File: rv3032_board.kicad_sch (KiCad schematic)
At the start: 7 parts, among them J1 Conn_01x05_Pin, U1 RV-3032

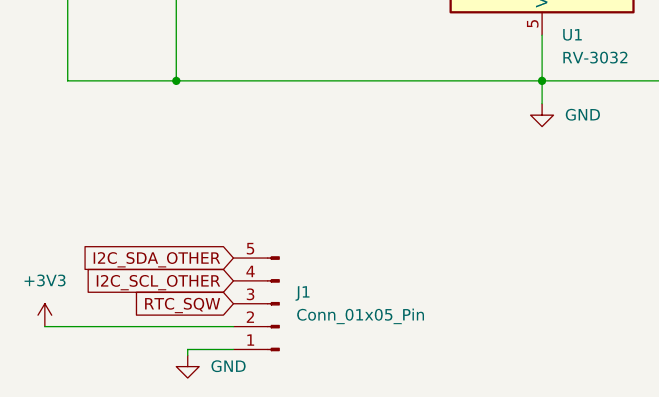
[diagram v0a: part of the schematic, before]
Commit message: v2: replacement DS3231
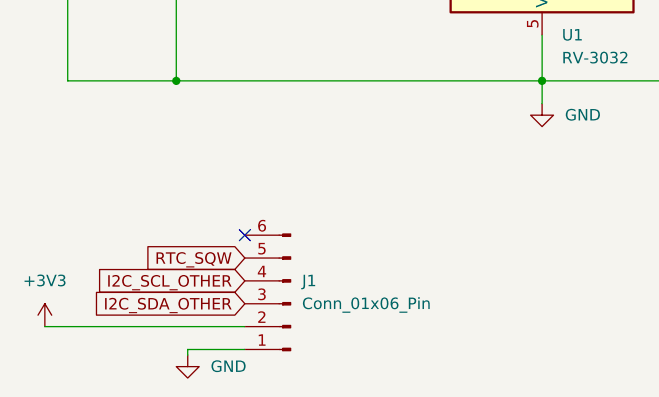
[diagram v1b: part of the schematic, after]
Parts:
- removed J1: Conn_01x05_Pin, Connector_PinHeader_2.54mm:PinHeader_1x05_P2.54mm_Horizontal, symbol Connector:Conn_01x05_Pin
- added J1: Conn_01x06_Pin, Connector_PinHeader_2.54mm:PinHeader_1x06_P2.54mm_Horizontal, symbol Connector:Conn_01x06_Pin
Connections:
- net +3V3: now also J1.2 (Pin_2)
- net GND: now also J1.1 (Pin_1)
- net I2C_SCL_OTHER: now also J1.4 (Pin_4)
- net I2C_SDA_OTHER: now also J1.3 (Pin_3)
- net RTC_SQW: now also J1.5 (Pin_5)
- no-connect marks 2 -> 3
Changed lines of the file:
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@@
   (no_connect (at 106.68 45.085))
   (no_connect (at 106.68 42.545))
+  (no_connect (at 60.96 74.93))
   (wire (pts (xy 93.98 57.785) (xy 93.98 52.705))
     (stroke (width 0) (type default))
@@
     (stroke (width 0) (type default))
   )
-  (wire (pts (xy 59.69 87.63) (xy 54.61 87.63))
+  (wire (pts (xy 54.61 87.63) (xy 60.96 87.63))
     (stroke (width 0) (type default))
   )
@@
     (stroke (width 0) (type default))
   )
-  (wire (pts (xy 38.735 85.09) (xy 59.69 85.09))
+  (wire (pts (xy 38.735 85.09) (xy 60.96 85.09))
     (stroke (width 0) (type default))
   )
@@
     (stroke (width 0) (type default))
   )
-  (global_label "I2C_SDA_OTHER" (shape input) (at 59.69 77.47 180) (fields_autoplaced)
+  (global_label "I2C_SDA_OTHER" (shape input) (at 60.96 82.55 180) (fields_autoplaced)
     (effects (font (size 1.27 1.27)) (justify right))
-    (property "Intersheetrefs" "${INTERSHEET_REFS}" (at 42.0696 77.47 0)
+    (property "Intersheetrefs" "${INTERSHEET_REFS}" (at 43.3396 82.55 0)
       (effects (font (size 1.27 1.27)) (justify right) hide)
     )
@@
     )
   )
-  (global_label "I2C_SCL_OTHER" (shape input) (at 59.69 80.01 180) (fields_autoplaced)
+  (global_label "I2C_SCL_OTHER" (shape input) (at 60.96 80.01 180) (fields_autoplaced)
     (effects (font (size 1.27 1.27)) (justify right))
-    (property "Intersheetrefs" "${INTERSHEET_REFS}" (at 42.1301 80.01 0)
+    (property "Intersheetrefs" "${INTERSHEET_REFS}" (at 43.4001 80.01 0)
       (effects (font (size 1.27 1.27)) (justify right) hide)
     )
@@
     )
   )
-  (global_label "RTC_SQW" (shape input) (at 59.69 82.55 180) (fields_autoplaced)
+  (global_label "RTC_SQW" (shape input) (at 60.96 77.47 180) (fields_autoplaced)
     (effects (font (size 1.27 1.27)) (justify right))
-    (property "Intersheetrefs" "${INTERSHEET_REFS}" (at 48.2382 82.55 0)
+    (property "Intersheetrefs" "${INTERSHEET_REFS}" (at 49.5082 77.47 0)
       (effects (font (size 1.27 1.27)) (justify right) hide)
     )
@@
     (property "Intersheetrefs" "${INTERSHEET_REFS}" (at 63.7201 40.005 0)
       (effects (font (size 1.27 1.27)) (justify right) hide)
+    )
+  )
+  (symbol (lib_id "Connector:Conn_01x06_Pin") (at 66.04 82.55 180) (unit 1)
+    (in_bom yes) (on_board yes) (dnp no) (fields_autoplaced)
+    (property "Reference" "J1" (at 67.31 80.01 0)
+      (effects (font (size 1.27 1.27)) (justify right))
+    )
+    (property "Value" "Conn_01x06_Pin" (at 67.31 82.55 0)
+      (effects (font (size 1.27 1.27)) (justify right))
+    )
+    (property "Footprint" "Connector_PinHeader_2.54mm:PinHeader_1x06_P2.54mm_Horizontal" (at 66.04 82.55 0)
+      (effects (font (size 1.27 1.27)) hide)
+    )
+    (property "Datasheet" "~" (at 66.04 82.55 0)
+      (effects (font (size 1.27 1.27)) hide)
+    )
+    (pin "6")
+    (pin "5")
+    (pin "4")
+    (pin "2")
+    (pin "3")
+    (pin "1")
+    (instances
+      (project "rv3032_board"
+        (path "/9e174d63-a755-42b8-958a-a2d4627128df"
+          (reference "J1") (unit 1)
+        )
+      )
     )
   )
@@
         )
       )
-    )
-  )
-  (symbol (lib_id "Connector:Conn_01x05_Pin") (at 64.77 82.55 180) (unit 1)
-    (in_bom no) (on_board yes) (dnp no) (fields_autoplaced)
-    (property "Reference" "J1" (at 66.675 81.28 0)
-      (effects (font (size 1.27 1.27)) (justify right))
-    )
-    (property "Value" "Conn_01x05_Pin" (at 66.675 83.82 0)
-      (effects (font (size 1.27 1.27)) (justify right))
-    )
-    (property "Footprint" "Connector_PinHeader_2.54mm:PinHeader_1x05_P2.54mm_Horizontal" (at 64.77 82.55 0)
-      (effects (font (size 1.27 1.27)) hide)
-    )
-    (property "Datasheet" "~" (at 64.77 82.55 0)
-      (effects (font (size 1.27 1.27)) hide)
-    )
-    (pin "4")
-    (pin "2")
-    (pin "5")
-    (pin "3")
-    (pin "1")
-    (instances
-      (project "rv3032_board"
-        (path "/9e174d63-a755-42b8-958a-a2d4627128df"
-          (reference "J1") (unit 1)
-        )
-      )

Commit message: v1 ordered
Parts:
- J1: now left out of the parts list
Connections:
- net RTC_INT: now reaches J1.6 (Pin_6)
- net RTC_INT: now also U1.3 (~{INT})
- no-connect marks 3 -> 1
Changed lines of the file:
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@@
   (junction (at 132.08 57.785) (diameter 0) (color 0 0 0 0)
   )
-  (no_connect (at 106.68 45.085))
   (no_connect (at 106.68 42.545))
-  (no_connect (at 60.96 74.93))
   (wire (pts (xy 93.98 57.785) (xy 93.98 52.705))
     (stroke (width 0) (type default))
@@
     )
   )
+  (global_label "RTC_INT" (shape input) (at 60.96 74.93 180) (fields_autoplaced)
+    (effects (font (size 1.27 1.27)) (justify right))
+    (property "Intersheetrefs" "${INTERSHEET_REFS}" (at 50.5967 74.93 0)
+      (effects (font (size 1.27 1.27)) (justify right) hide)
+    )
+  )
+  (global_label "RTC_INT" (shape input) (at 106.68 45.085 0) (fields_autoplaced)
+    (effects (font (size 1.27 1.27)) (justify left))
+    (property "Intersheetrefs" "${INTERSHEET_REFS}" (at 117.0433 45.085 0)
+      (effects (font (size 1.27 1.27)) (justify left) hide)
+    )
+  )
   (global_label "I2C_SDA_OTHER" (shape input) (at 81.28 45.085 180) (fields_autoplaced)
     (effects (font (size 1.27 1.27)) (justify right))
@@
   )
   (symbol (lib_id "Connector:Conn_01x06_Pin") (at 66.04 82.55 180) (unit 1)
-    (in_bom yes) (on_board yes) (dnp no) (fields_autoplaced)
+    (in_bom no) (on_board yes) (dnp no) (fields_autoplaced)
     (property "Reference" "J1" (at 67.31 80.01 0)
       (effects (font (size 1.27 1.27)) (justify right))
